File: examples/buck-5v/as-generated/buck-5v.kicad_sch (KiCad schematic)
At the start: 18 parts, among them J1 12V IN, J2 5V OUT, U1 LM2596S-5

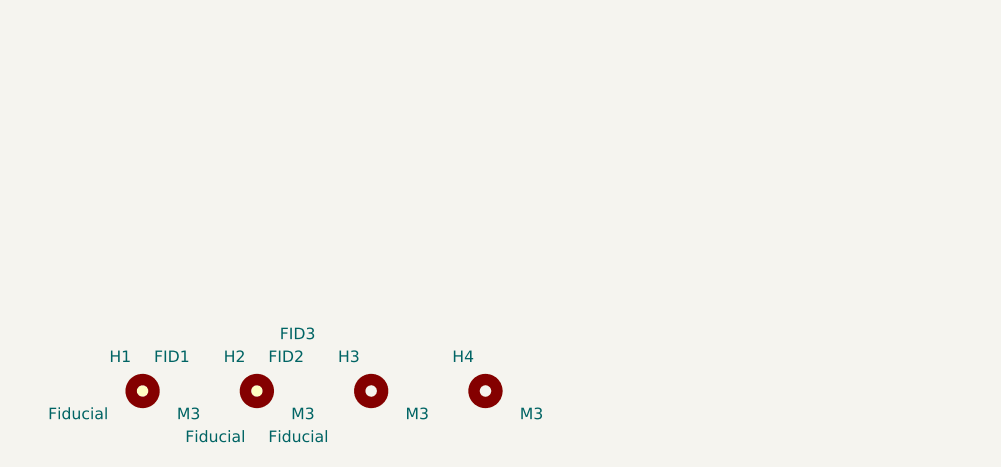
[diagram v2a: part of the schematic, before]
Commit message: Let the new parts sit somewhere sensible, on the board and on the sheet
Placing screw holes and fiducials turned up four things that were wrong
before either existed, all of them about where something is allowed to
go rather than about the parts themselves.

A designator was kept off the pads but not inside the board outline, so
any part at the edge - a connector, and now a hole - had its reference
clipped by the edge. Every board had been carrying one or two of those.

A symbol with no pins leaves no trace in the sheet planner's obstacle
list, because that list is built from pin stubs. The screw holes were
invisible to it and the fiducials landed on top of them. The free-row
search also ran off the right-hand edge of an A4 page and sat over the
title block on the way, which is `readability.outside_page` and
`readability.margin_intrusion` respectively - both real, both now
avoided by bounding the search to the drawing area.

And the bill-of-materials flag is read from the footprint rather than
the symbol library, because the footprint is the side KiCad's parity
check reads and the side the fab agrees with. That retired three
warnings the op-amp board had been carrying since it gained test
points: `Connector:TestPoint` claims to be a BOM line and its own
footprint says otherwise.

All four fast boards pass their gates; the suite is green on 10.0.4.

Co-Authored-By: Claude Fable 5 <noreply@anthropic.com>
Claude-Session: https://claude.ai/code/session_01DUj7Ltu92tWg159mCSacwY
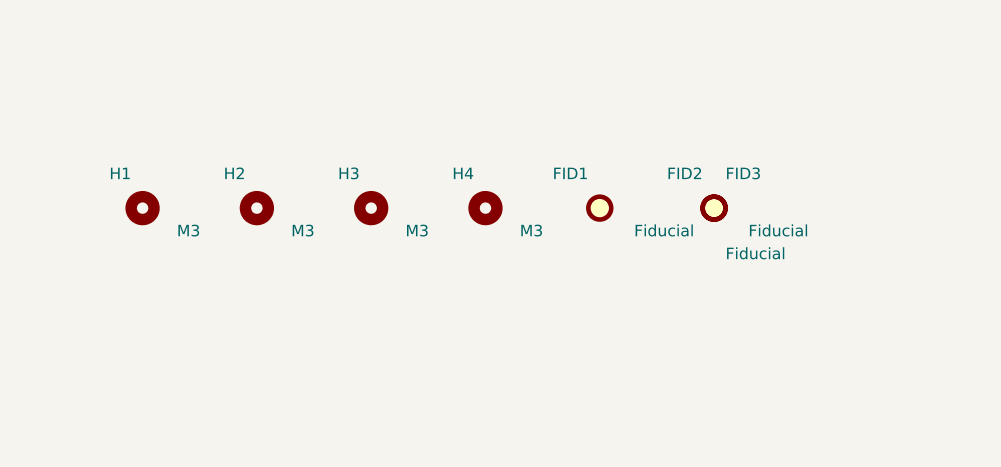
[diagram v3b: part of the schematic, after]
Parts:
- FID1, FID2, FID3, H1, H2, H3, H4: now left out of the parts list
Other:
- moved on the sheet: FID1, FID2, FID3, H1, H2, H3, H4
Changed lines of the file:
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@@
     (instances (project "buck-5v" (path "/ec98644d-848c-5056-a4cb-c829189be5c3" (reference "J2") (unit 1))))
   )
-  (symbol (lib_id "Mechanical:MountingHole") (at 25.71 169.99 0.0) (unit 1)
-    (exclude_from_sim no) (in_bom yes) (on_board yes) (dnp no)
-    (property "Reference" "H1" (at 24.44 166.18 0) (effects (font (size 1.27 1.27)) (justify right)))
-    (property "Value" "M3" (at 29.52 172.53 0) (effects (font (size 1.27 1.27)) (justify left)))
-    (property "Footprint" "MountingHole:MountingHole_3.2mm_M3" (at 25.71 169.99 0) (effects (font (size 1.27 1.27)) hide))
-    (property "Datasheet" "~" (at 25.71 169.99 0) (effects (font (size 1.27 1.27)) hide))
+  (symbol (lib_id "Mechanical:MountingHole") (at 25.71 149.67 0.0) (unit 1)
+    (exclude_from_sim no) (in_bom no) (on_board yes) (dnp no)
+    (property "Reference" "H1" (at 24.44 145.86 0) (effects (font (size 1.27 1.27)) (justify right)))
+    (property "Value" "M3" (at 29.52 152.21 0) (effects (font (size 1.27 1.27)) (justify left)))
+    (property "Footprint" "MountingHole:MountingHole_3.2mm_M3" (at 25.71 149.67 0) (effects (font (size 1.27 1.27)) hide))
+    (property "Datasheet" "~" (at 25.71 149.67 0) (effects (font (size 1.27 1.27)) hide))
     (instances (project "buck-5v" (path "/ec98644d-848c-5056-a4cb-c829189be5c3" (reference "H1") (unit 1))))
   )
-  (symbol (lib_id "Mechanical:MountingHole") (at 38.41 169.99 0.0) (unit 1)
-    (exclude_from_sim no) (in_bom yes) (on_board yes) (dnp no)
-    (property "Reference" "H2" (at 37.14 166.18 0) (effects (font (size 1.27 1.27)) (justify right)))
-    (property "Value" "M3" (at 42.22 172.53 0) (effects (font (size 1.27 1.27)) (justify left)))
-    (property "Footprint" "MountingHole:MountingHole_3.2mm_M3" (at 38.41 169.99 0) (effects (font (size 1.27 1.27)) hide))
-    (property "Datasheet" "~" (at 38.41 169.99 0) (effects (font (size 1.27 1.27)) hide))
+  (symbol (lib_id "Mechanical:MountingHole") (at 38.41 149.67 0.0) (unit 1)
+    (exclude_from_sim no) (in_bom no) (on_board yes) (dnp no)
+    (property "Reference" "H2" (at 37.14 145.86 0) (effects (font (size 1.27 1.27)) (justify right)))
+    (property "Value" "M3" (at 42.22 152.21 0) (effects (font (size 1.27 1.27)) (justify left)))
+    (property "Footprint" "MountingHole:MountingHole_3.2mm_M3" (at 38.41 149.67 0) (effects (font (size 1.27 1.27)) hide))
+    (property "Datasheet" "~" (at 38.41 149.67 0) (effects (font (size 1.27 1.27)) hide))
     (instances (project "buck-5v" (path "/ec98644d-848c-5056-a4cb-c829189be5c3" (reference "H2") (unit 1))))
   )
-  (symbol (lib_id "Mechanical:MountingHole") (at 51.11 169.99 0.0) (unit 1)
-    (exclude_from_sim no) (in_bom yes) (on_board yes) (dnp no)
-    (property "Reference" "H3" (at 49.84 166.18 0) (effects (font (size 1.27 1.27)) (justify right)))
-    (property "Value" "M3" (at 54.92 172.53 0) (effects (font (size 1.27 1.27)) (justify left)))
-    (property "Footprint" "MountingHole:MountingHole_3.2mm_M3" (at 51.11 169.99 0) (effects (font (size 1.27 1.27)) hide))
-    (property "Datasheet" "~" (at 51.11 169.99 0) (effects (font (size 1.27 1.27)) hide))
+  (symbol (lib_id "Mechanical:MountingHole") (at 51.11 149.67 0.0) (unit 1)
+    (exclude_from_sim no) (in_bom no) (on_board yes) (dnp no)
+    (property "Reference" "H3" (at 49.84 145.86 0) (effects (font (size 1.27 1.27)) (justify right)))
+    (property "Value" "M3" (at 54.92 152.21 0) (effects (font (size 1.27 1.27)) (justify left)))
+    (property "Footprint" "MountingHole:MountingHole_3.2mm_M3" (at 51.11 149.67 0) (effects (font (size 1.27 1.27)) hide))
+    (property "Datasheet" "~" (at 51.11 149.67 0) (effects (font (size 1.27 1.27)) hide))
     (instances (project "buck-5v" (path "/ec98644d-848c-5056-a4cb-c829189be5c3" (reference "H3") (unit 1))))
   )
-  (symbol (lib_id "Mechanical:MountingHole") (at 63.81 169.99 0.0) (unit 1)
-    (exclude_from_sim no) (in_bom yes) (on_board yes) (dnp no)
-    (property "Reference" "H4" (at 62.54 166.18 0) (effects (font (size 1.27 1.27)) (justify right)))
-    (property "Value" "M3" (at 67.62 172.53 0) (effects (font (size 1.27 1.27)) (justify left)))
-    (property "Footprint" "MountingHole:MountingHole_3.2mm_M3" (at 63.81 169.99 0) (effects (font (size 1.27 1.27)) hide))
-    (property "Datasheet" "~" (at 63.81 169.99 0) (effects (font (size 1.27 1.27)) hide))
+  (symbol (lib_id "Mechanical:MountingHole") (at 63.81 149.67 0.0) (unit 1)
+    (exclude_from_sim no) (in_bom no) (on_board yes) (dnp no)
+    (property "Reference" "H4" (at 62.54 145.86 0) (effects (font (size 1.27 1.27)) (justify right)))
+    (property "Value" "M3" (at 67.62 152.21 0) (effects (font (size 1.27 1.27)) (justify left)))
+    (property "Footprint" "MountingHole:MountingHole_3.2mm_M3" (at 63.81 149.67 0) (effects (font (size 1.27 1.27)) hide))
+    (property "Datasheet" "~" (at 63.81 149.67 0) (effects (font (size 1.27 1.27)) hide))
     (instances (project "buck-5v" (path "/ec98644d-848c-5056-a4cb-c829189be5c3" (reference "H4") (unit 1))))
   )
-  (symbol (lib_id "Mechanical:Fiducial") (at 25.71 169.99 0.0) (unit 1)
-    (exclude_from_sim no) (in_bom yes) (on_board yes) (dnp no)
-    (property "Reference" "FID1" (at 26.98 166.18 0) (effects (font (size 1.27 1.27)) (justify left)))
-    (property "Value" "Fiducial" (at 21.9 172.53 0) (effects (font (size 1.27 1.27)) (justify right)))
-    (property "Footprint" "Fiducial:Fiducial_1mm_Mask2mm" (at 25.71 169.99 0) (effects (font (size 1.27 1.27)) hide))
-    (property "Datasheet" "~" (at 25.71 169.99 0) (effects (font (size 1.27 1.27)) hide))
+  (symbol (lib_id "Mechanical:Fiducial") (at 76.51 149.67 0.0) (unit 1)
+    (exclude_from_sim no) (in_bom no) (on_board yes) (dnp no)
+    (property "Reference" "FID1" (at 75.24 145.86 0) (effects (font (size 1.27 1.27)) (justify right)))
+    (property "Value" "Fiducial" (at 80.32 152.21 0) (effects (font (size 1.27 1.27)) (justify left)))
+    (property "Footprint" "Fiducial:Fiducial_1mm_Mask2mm" (at 76.51 149.67 0) (effects (font (size 1.27 1.27)) hide))
+    (property "Datasheet" "~" (at 76.51 149.67 0) (effects (font (size 1.27 1.27)) hide))
     (instances (project "buck-5v" (path "/ec98644d-848c-5056-a4cb-c829189be5c3" (reference "FID1") (unit 1))))
   )
-  (symbol (lib_id "Mechanical:Fiducial") (at 38.41 169.99 0.0) (unit 1)
-    (exclude_from_sim no) (in_bom yes) (on_board yes) (dnp no)
-    (property "Reference" "FID2" (at 39.68 166.18 0) (effects (font (size 1.27 1.27)) (justify left)))
-    (property "Value" "Fiducial" (at 39.68 175.07 0) (effects (font (size 1.27 1.27)) (justify left)))
-    (property "Footprint" "Fiducial:Fiducial_1mm_Mask2mm" (at 38.41 169.99 0) (effects (font (size 1.27 1.27)) hide))
-    (property "Datasheet" "~" (at 38.41 169.99 0) (effects (font (size 1.27 1.27)) hide))
+  (symbol (lib_id "Mechanical:Fiducial") (at 89.21 149.67 0.0) (unit 1)
+    (exclude_from_sim no) (in_bom no) (on_board yes) (dnp no)
+    (property "Reference" "FID2" (at 87.94 145.86 0) (effects (font (size 1.27 1.27)) (justify right)))
+    (property "Value" "Fiducial" (at 93.02 152.21 0) (effects (font (size 1.27 1.27)) (justify left)))
+    (property "Footprint" "Fiducial:Fiducial_1mm_Mask2mm" (at 89.21 149.67 0) (effects (font (size 1.27 1.27)) hide))
+    (property "Datasheet" "~" (at 89.21 149.67 0) (effects (font (size 1.27 1.27)) hide))
     (instances (project "buck-5v" (path "/ec98644d-848c-5056-a4cb-c829189be5c3" (reference "FID2") (unit 1))))
   )
-  (symbol (lib_id "Mechanical:Fiducial") (at 38.41 169.99 0.0) (unit 1)
-    (exclude_from_sim no) (in_bom yes) (on_board yes) (dnp no)
-    (property "Reference" "FID3" (at 40.95 163.64 0) (effects (font (size 1.27 1.27)) (justify left)))
-    (property "Value" "Fiducial" (at 37.14 175.07 0) (effects (font (size 1.27 1.27)) (justify right)))
-    (property "Footprint" "Fiducial:Fiducial_1mm_Mask2mm" (at 38.41 169.99 0) (effects (font (size 1.27 1.27)) hide))
-    (property "Datasheet" "~" (at 38.41 169.99 0) (effects (font (size 1.27 1.27)) hide))
+  (symbol (lib_id "Mechanical:Fiducial") (at 89.21 149.67 0.0) (unit 1)
+    (exclude_from_sim no) (in_bom no) (on_board yes) (dnp no)
+    (property "Reference" "FID3" (at 90.48 145.86 0) (effects (font (size 1.27 1.27)) (justify left)))
+    (property "Value" "Fiducial" (at 90.48 154.75 0) (effects (font (size 1.27 1.27)) (justify left)))
+    (property "Footprint" "Fiducial:Fiducial_1mm_Mask2mm" (at 89.21 149.67 0) (effects (font (size 1.27 1.27)) hide))
+    (property "Datasheet" "~" (at 89.21 149.67 0) (effects (font (size 1.27 1.27)) hide))
     (instances (project "buck-5v" (path "/ec98644d-848c-5056-a4cb-c829189be5c3" (reference "FID3") (unit 1))))
   )

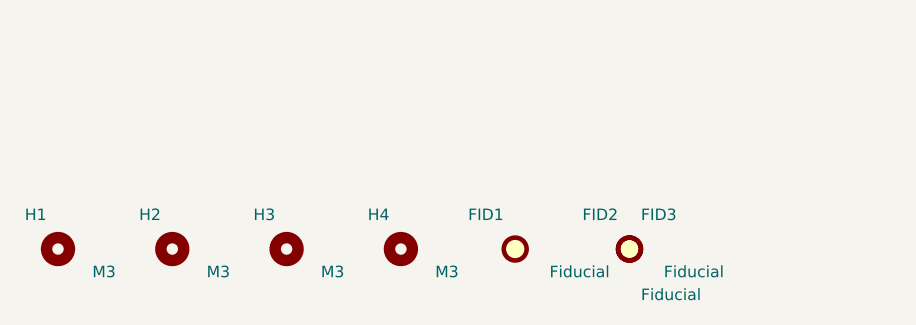
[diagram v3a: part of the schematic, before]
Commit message: Put the vias back where the copper moved, and let the fillets vote
The FPGA board came back from its re-route with two unconnected nets and
three dangling ends, and the cause was older than anything this round
added. The router hands back a via for every layer change; six passes
then reshape the copper - snapping to 45s, chamfering, spreading folds,
and now filleting - and none of them move the holes underneath. A joint
that slides a millimetre from its via is two loose ends and one broken
net, and `_unlooped` then swept the via away as orphaned, because it
kept a via only when a track ended on its exact coordinate.

Two fixes, both about what "connected" means. A via lives if kept copper
*touches* it, not if a coordinate matches. And a new `_joined` pass
re-derives the joints from the copper that actually got written: where a
net ends on two layers at one point with no via reaching it, one goes
back in. It reads the finished geometry, so it cannot drift the way six
separate passes carrying vias along with them would.

The same reasoning fixes two rules that had been measuring coordinates
rather than copper. `route.stub` matched a track end to a via's centre
exactly, and called a joint a stub whenever a reshaping pass had moved
it a quarter of a millimetre inside the very barrel it was connected to.
`route.width_step` walked a neck back to its pad and stopped at the
first width change - which, on a filleted board, is the teardrop, so
every escape's neck stopped being recognised as one.

While the three copies of the post-route pipeline were being edited for
the third time this session, they became one function. That is how
`_teardrops` had come to run on two of the three exits.

All five boards: DRC clean on both matrix versions, nothing unconnected.
Four pass their gates; the FPGA board is down to the two-layer bill it
has always had - four nets over plane cuts and one 88 degree corner.

Co-Authored-By: Claude Fable 5 <noreply@anthropic.com>
Claude-Session: https:/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
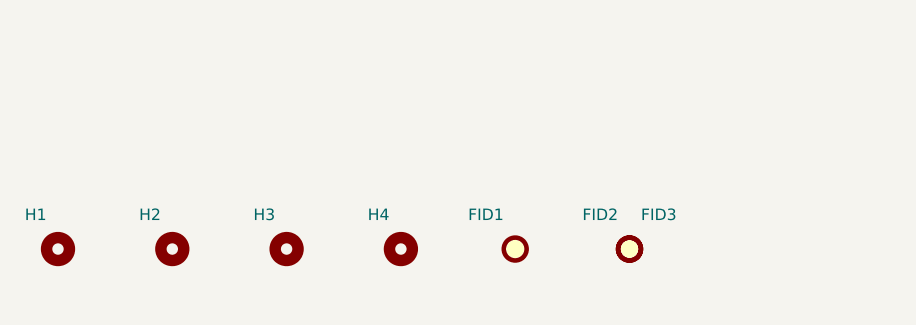
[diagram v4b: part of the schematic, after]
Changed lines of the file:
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@@
     (exclude_from_sim no) (in_bom no) (on_board yes) (dnp no)
     (property "Reference" "H1" (at 24.44 145.86 0) (effects (font (size 1.27 1.27)) (justify right)))
-    (property "Value" "M3" (at 29.52 152.21 0) (effects (font (size 1.27 1.27)) (justify left)))
+    (property "Value" "M3" (at 29.52 152.21 0) (effects (font (size 1.27 1.27)) (justify left) hide))
     (property "Footprint" "MountingHole:MountingHole_3.2mm_M3" (at 25.71 149.67 0) (effects (font (size 1.27 1.27)) hide))
     (property "Datasheet" "~" (at 25.71 149.67 0) (effects (font (size 1.27 1.27)) hide))
@@
     (exclude_from_sim no) (in_bom no) (on_board yes) (dnp no)
     (property "Reference" "H2" (at 37.14 145.86 0) (effects (font (size 1.27 1.27)) (justify right)))
-    (property "Value" "M3" (at 42.22 152.21 0) (effects (font (size 1.27 1.27)) (justify left)))
+    (property "Value" "M3" (at 42.22 152.21 0) (effects (font (size 1.27 1.27)) (justify left) hide))
     (property "Footprint" "MountingHole:MountingHole_3.2mm_M3" (at 38.41 149.67 0) (effects (font (size 1.27 1.27)) hide))
     (property "Datasheet" "~" (at 38.41 149.67 0) (effects (font (size 1.27 1.27)) hide))
@@
     (exclude_from_sim no) (in_bom no) (on_board yes) (dnp no)
     (property "Reference" "H3" (at 49.84 145.86 0) (effects (font (size 1.27 1.27)) (justify right)))
-    (property "Value" "M3" (at 54.92 152.21 0) (effects (font (size 1.27 1.27)) (justify left)))
+    (property "Value" "M3" (at 54.92 152.21 0) (effects (font (size 1.27 1.27)) (justify left) hide))
     (property "Footprint" "MountingHole:MountingHole_3.2mm_M3" (at 51.11 149.67 0) (effects (font (size 1.27 1.27)) hide))
     (property "Datasheet" "~" (at 51.11 149.67 0) (effects (font (size 1.27 1.27)) hide))
@@
     (exclude_from_sim no) (in_bom no) (on_board yes) (dnp no)
     (property "Reference" "H4" (at 62.54 145.86 0) (effects (font (size 1.27 1.27)) (justify right)))
-    (property "Value" "M3" (at 67.62 152.21 0) (effects (font (size 1.27 1.27)) (justify left)))
+    (property "Value" "M3" (at 67.62 152.21 0) (effects (font (size 1.27 1.27)) (justify left) hide))
     (property "Footprint" "MountingHole:MountingHole_3.2mm_M3" (at 63.81 149.67 0) (effects (font (size 1.27 1.27)) hide))
     (property "Datasheet" "~" (at 63.81 149.67 0) (effects (font (size 1.27 1.27)) hide))
@@
     (exclude_from_sim no) (in_bom no) (on_board yes) (dnp no)
     (property "Reference" "FID1" (at 75.24 145.86 0) (effects (font (size 1.27 1.27)) (justify right)))
-    (property "Value" "Fiducial" (at 80.32 152.21 0) (effects (font (size 1.27 1.27)) (justify left)))
+    (property "Value" "Fiducial" (at 80.32 152.21 0) (effects (font (size 1.27 1.27)) (justify left) hide))
     (property "Footprint" "Fiducial:Fiducial_1mm_Mask2mm" (at 76.51 149.67 0) (effects (font (size 1.27 1.27)) hide))
     (property "Datasheet" "~" (at 76.51 149.67 0) (effects (font (size 1.27 1.27)) hide))
@@
     (exclude_from_sim no) (in_bom no) (on_board yes) (dnp no)
     (property "Reference" "FID2" (at 87.94 145.86 0) (effects (font (size 1.27 1.27)) (justify right)))
-    (property "Value" "Fiducial" (at 93.02 152.21 0) (effects (font (size 1.27 1.27)) (justify left)))
+    (property "Value" "Fiducial" (at 93.02 152.21 0) (effects (font (size 1.27 1.27)) (justify left) hide))
     (property "Footprint" "Fiducial:Fiducial_1mm_Mask2mm" (at 89.21 149.67 0) (effects (font (size 1.27 1.27)) hide))
     (property "Datasheet" "~" (at 89.21 149.67 0) (effects (font (size 1.27 1.27)) hide))
@@
     (exclude_from_sim no) (in_bom no) (on_board yes) (dnp no)
     (property "Reference" "FID3" (at 90.48 145.86 0) (effects (font (size 1.27 1.27)) (justify left)))
-    (property "Value" "Fiducial" (at 90.48 154.75 0) (effects (font (size 1.27 1.27)) (justify left)))
+    (property "Value" "Fiducial" (at 90.48 154.75 0) (effects (font (size 1.27 1.27)) (justify left) hide))
     (property "Footprint" "Fiducial:Fiducial_1mm_Mask2mm" (at 89.21 149.67 0) (effects (font (size 1.27 1.27)) hide))
     (property "Datasheet" "~" (at 89.21 149.67 0) (effects (font (size 1.27 1.27)) hide))
